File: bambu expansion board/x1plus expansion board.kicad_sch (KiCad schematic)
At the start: 25 parts, among them CN1 USB-CON-AF-MH4, CN2 USB-CON-AF-MH4, CN3 USB-CON-AF-MH4, U1 LAN9514-JZX-TR, U2 TPS54202DDCR, U3 AMS1117-3.3, U4 HC913550A-M899-A, U5 FT2232HL

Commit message: datasheets
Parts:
- removed CN3: USB-CON-AF-MH4, easyeda2kicad:USB-A-SMD_AF-MH4, symbol easyeda2kicad:USB-CON-AF-MH4
- removed D3: USBLC6-2P6_C2827693, easyeda2kicad:SOT-666-6_L1.6-W1.2-P0.50-LS1.6-BL, symbol easyeda2kicad:USBLC6-2P6_C2827693
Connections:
- net USBDM5: no longer U1.8 (USBDM5)
- net USBDP5: no longer U1.9 (USBDP5)
- net X1_CAM_DM: now also U1.8 (USBDM5)
- net X1_CAM_DP: now also U1.9 (USBDP5)

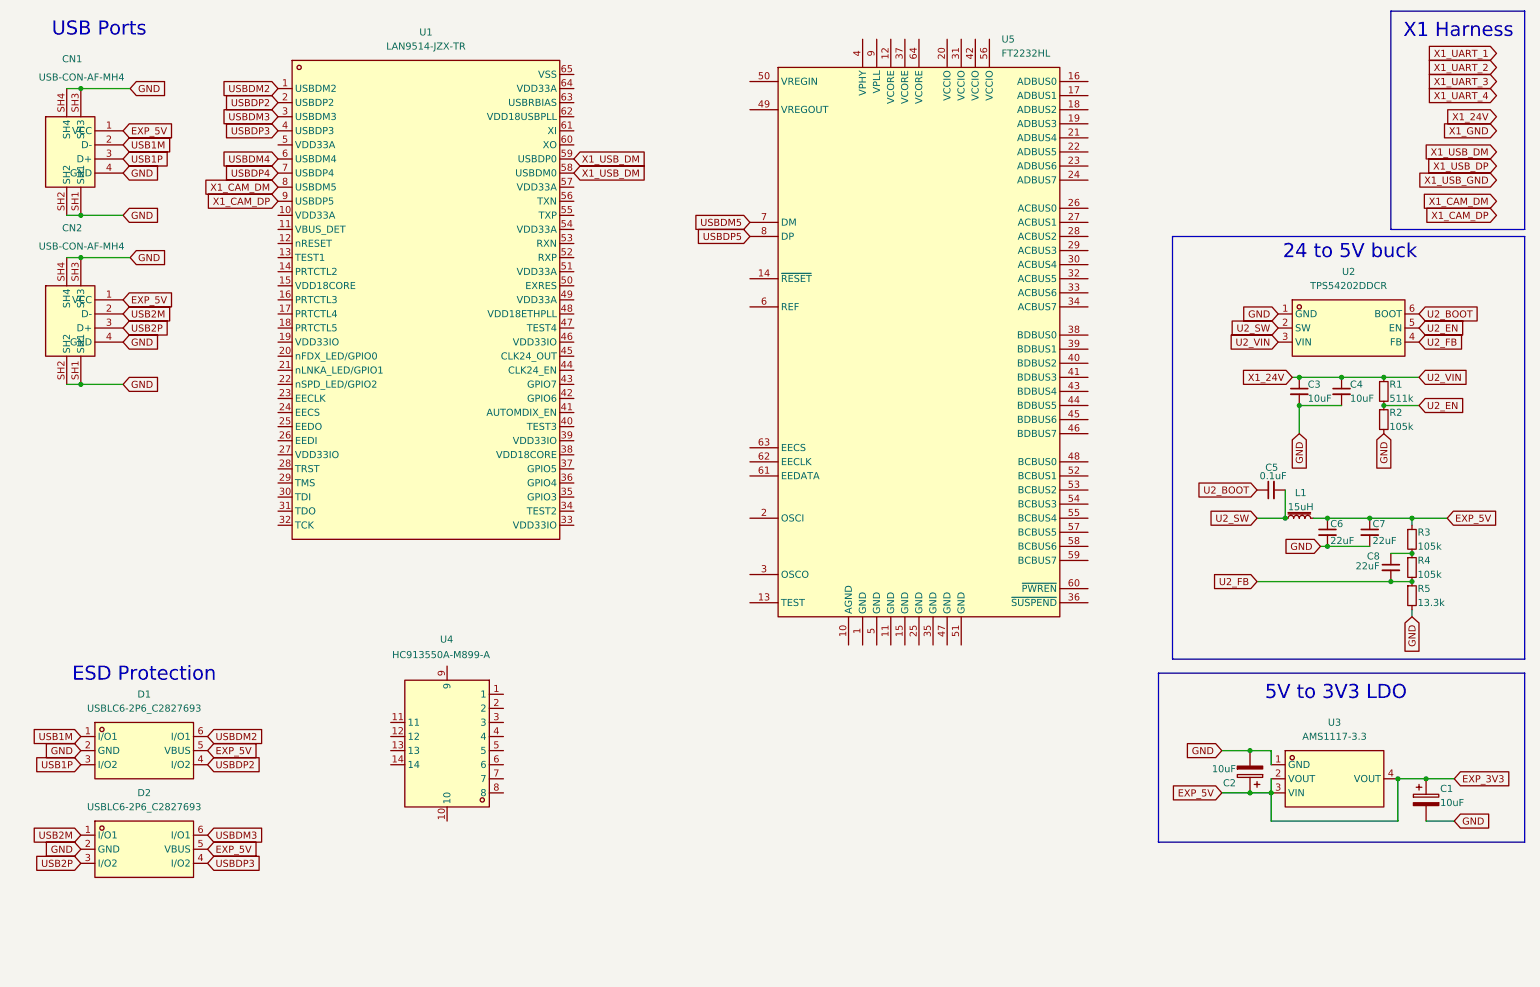
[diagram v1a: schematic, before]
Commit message: datasheets, correct wiring error
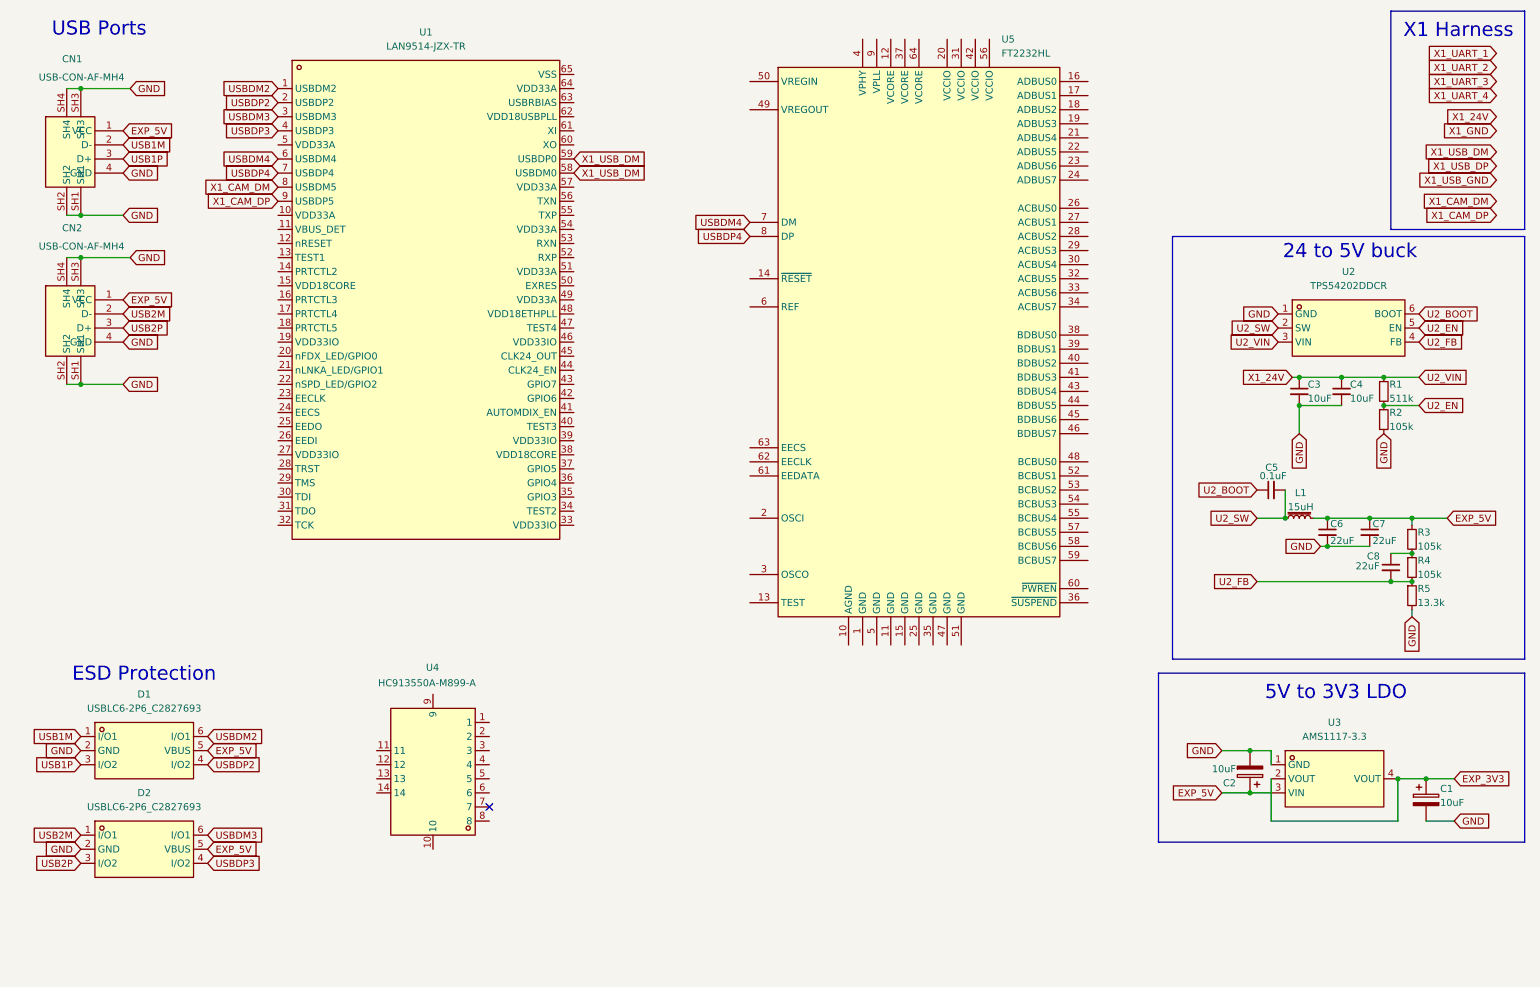
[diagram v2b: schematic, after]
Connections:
- net USBDM5 is gone; now on net USBDM4: U5.7 (DM)
- net USBDP5 is gone; now on net USBDP4: U5.8 (DP)
- net EXP_3V3: no longer C2.1, C6.1, C7.1, CN1.1 (VCC), CN2.1 (VCC), D1.5 (VBUS), D2.5 (VBUS), L1.2, R3.1, U3.3 (VIN)
- new net EXP_5V: C2.1, C6.1, C7.1, CN1.1 (VCC), CN2.1 (VCC), D1.5 (VBUS), D2.5 (VBUS), L1.2, R3.1, U3.3 (VIN)
- no-connect marks 0 -> 1
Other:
- moved on the sheet: U4
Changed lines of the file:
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@@
-	)
-	(junction
-		(at 238.76 153.67)
-		(diameter 0)
-		(color 0 0 0 0)
 	)
 	(junction
@@
 		(color 0 0 0 0)
 	)
+	(no_connect
+		(at 97.79 156.21)
+	)
 	(wire
 		(pts
@@
 	(wire
 		(pts
-			(xy 238.76 151.13) (xy 238.76 153.67)
+			(xy 238.76 151.13) (xy 238.76 158.75)
 		)
 		(stroke
@@
 		(pts
 			(xy 248.92 109.22) (xy 256.54 109.22)
-		)
-		(stroke
-			(width 0)
-			(type default)
-		)
-	)
-	(wire
-		(pts
-			(xy 238.76 153.67) (xy 238.76 158.75)
 		)
 		(stroke
@@
 		)
 	)
-	(global_label "USBDM5"
+	(global_label "USBDM4"
 		(shape input)
 		(at 144.78 50.8 180)
@@
 		)
 	)
-	(global_label "USBDP5"
+	(global_label "USBDP4"
 		(shape input)
 		(at 144.78 53.34 180)
@@
 	(symbol
 		(lib_id "easyeda2kicad:HC913550A-M899-A")
-		(at 90.17 144.78 270)
+		(at 87.63 149.86 270)
 		(unit 1)
 		(exclude_from_sim no)
@@
 		(dnp no)
 		(property "Reference" "U4"
-			(at 88.9 125.984 90)
+			(at 86.36 131.064 90)
 			(effects
 				(font
@@
 		)
 		(property "Value" "HC913550A-M899-A"
-			(at 80.264 128.778 90)
+			(at 77.724 133.858 90)
 			(effects
 				(font
@@
 		)
 		(property "Footprint" "easyeda2kicad:RJ45-TH_HC913550A-M899-A"
-			(at 72.39 144.78 0)
+			(at 69.85 149.86 0)
 			(effects
 				(font
@@
 		)
 		(property "Datasheet" ""
-			(at 90.17 144.78 0)
+			(at 87.63 149.86 0)
 			(effects
 				(font
@@
 		)
 		(property "Description" ""
-			(at 90.17 144.78 0)
+			(at 87.63 149.86 0)
 			(effects
 				(font
@@
 		)
 		(property "LCSC Part" "C3021374"
-			(at 69.85 144.78 0)
-			(effects
-				(font
+			(at 67.31 149.86 0)
+			(effects
+				(font
